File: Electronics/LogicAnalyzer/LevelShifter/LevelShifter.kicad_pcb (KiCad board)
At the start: 2 copper layers, 28.3 x 39.8 mm, 20 parts, among them J1 Conn_02x15_Odd_Even, J2 Conn_02x15_Odd_Even, U1 TXU0104PWR, U2 TXU0104PWR, U3 TXU0104PWR, U4 TXU0104PWR, U5 TXU0104PWR, U6 TXU0104PWR

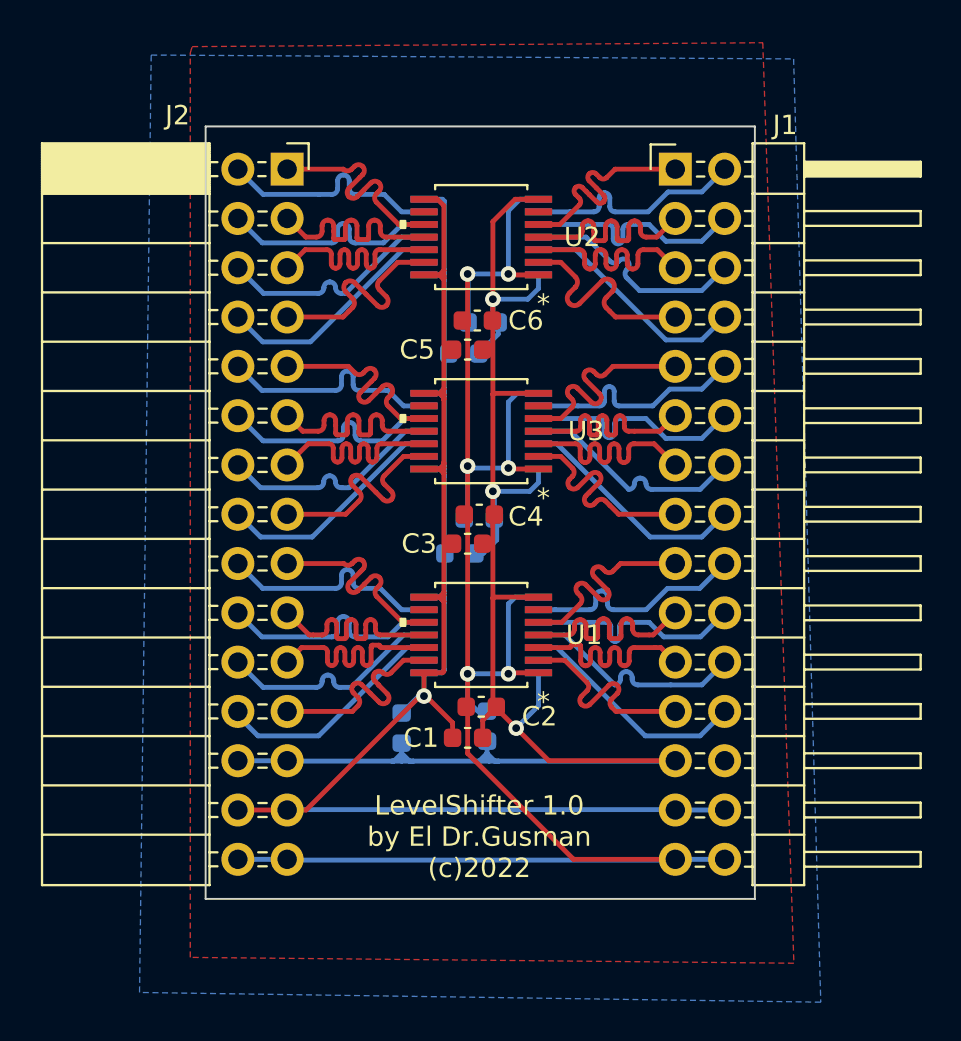
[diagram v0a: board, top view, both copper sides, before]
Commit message: Updated shifter board
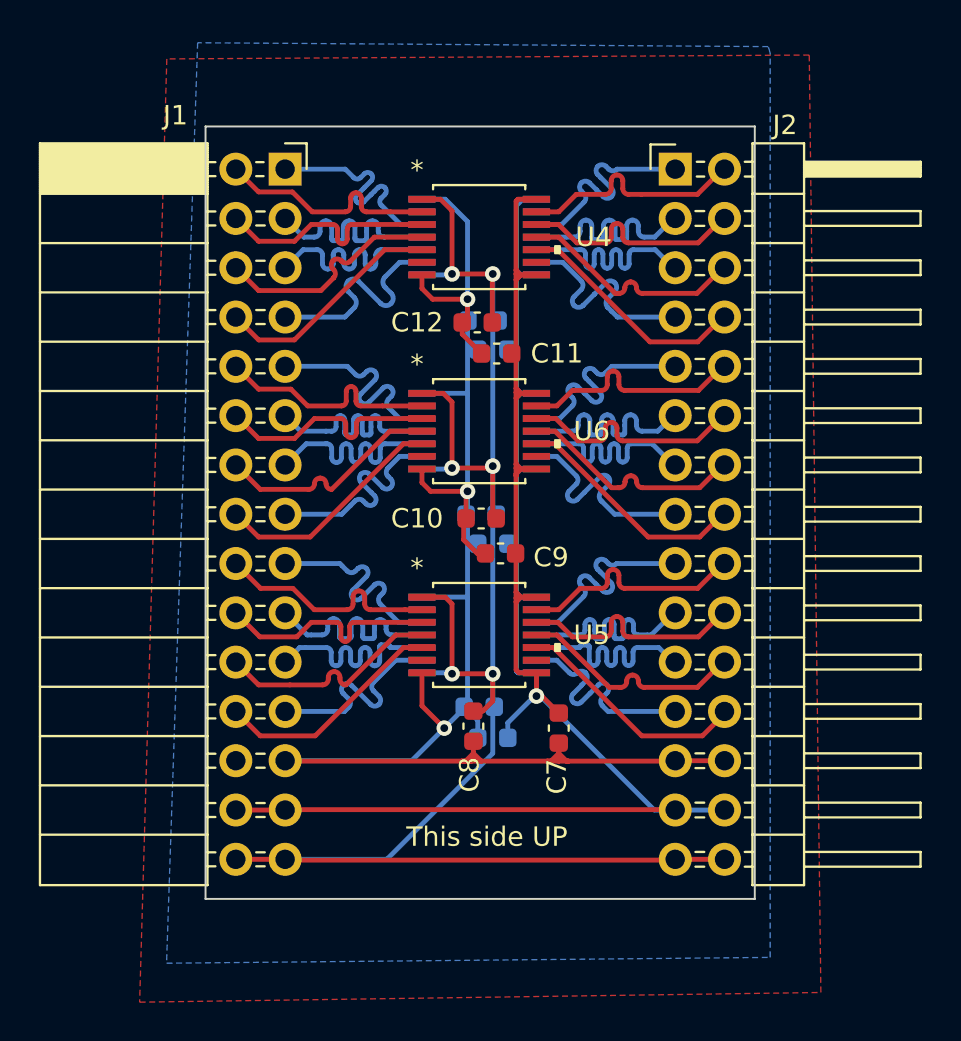
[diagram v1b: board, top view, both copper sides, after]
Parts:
- C1, C2, C3, C4, C5, C6, U1, U2, U3: moved to B.Cu
- C10, C11, C12, C7, C8, C9, U4, U5, U6: moved to F.Cu
- J1: footprint Connector_PinHeader_2.54mm:PinHeader_2x15_P2.54mm_Horizontal -> Connector_PinSocket_2.54mm:PinSocket_2x15_P2.54mm_Horizontal
- J2: footprint Connector_PinSocket_2.54mm:PinSocket_2x15_P2.54mm_Horizontal -> Connector_PinHeader_2.54mm:PinHeader_2x15_P2.54mm_Horizontal
- moved J1 20.1 mm to (149.9, 80.0)
- moved J2 20.0 mm to (170.0, 80.0)
- moved C7 8.09 mm to (164.0, 108.8)
- moved C9 2.09 mm to (161.0, 99.8), turned to 180 degrees
- moved C11 1.69 mm to (160.8, 89.5), turned to 180 degrees
- moved C1 1.29 mm to (160.6, 109.3), turned to 180 degrees
- moved C3 1.29 mm to (160.6, 99.3), turned to 180 degrees
- moved C5 1.29 mm to (160.6, 89.3), turned to 180 degrees
- moved C8 0.71 mm to (159.6, 108.7)
- moved C12 0.31 mm to (159.8, 87.9), turned to 0 degrees
- moved C6 0.29 mm to (160.1, 87.8), turned to 0 degrees
- moved C2 0.10 mm to (159.9, 107.7), turned to 0 degrees
- moved U1 0.10 mm to (159.9, 104.0), turned to 0 degrees
- moved U2 0.10 mm to (159.9, 83.5), turned to 0 degrees
- moved U3 0.10 mm to (159.9, 93.5), turned to 0 degrees
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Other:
- board text added: "This side UP"

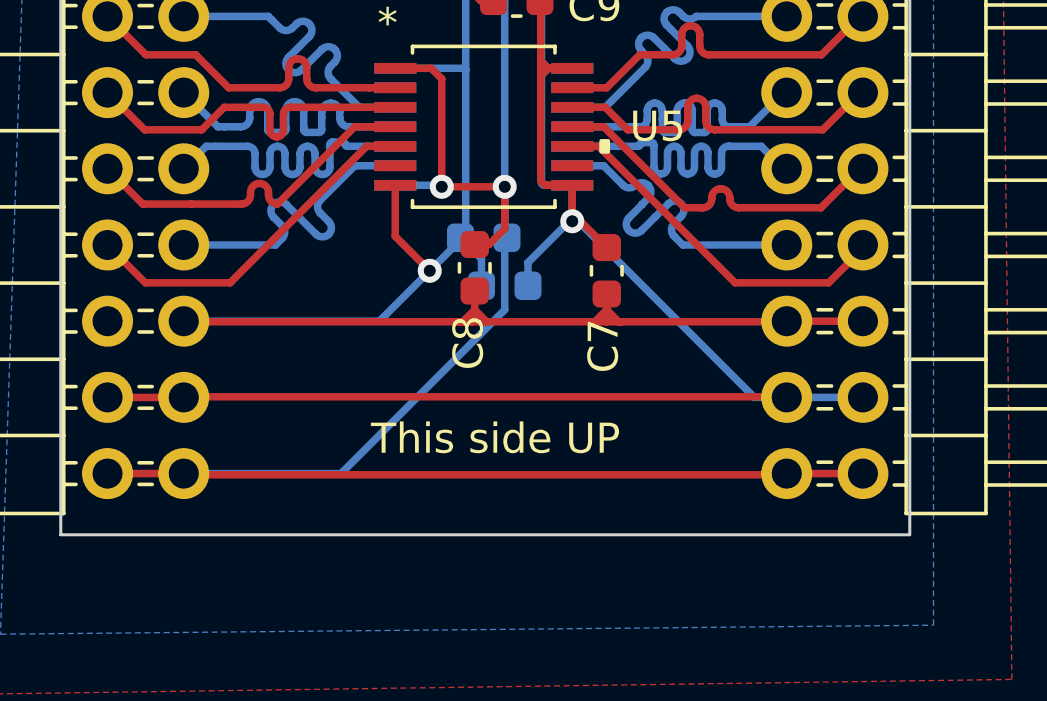
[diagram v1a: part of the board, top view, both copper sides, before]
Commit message: Updated LevelShifter with VRef selector
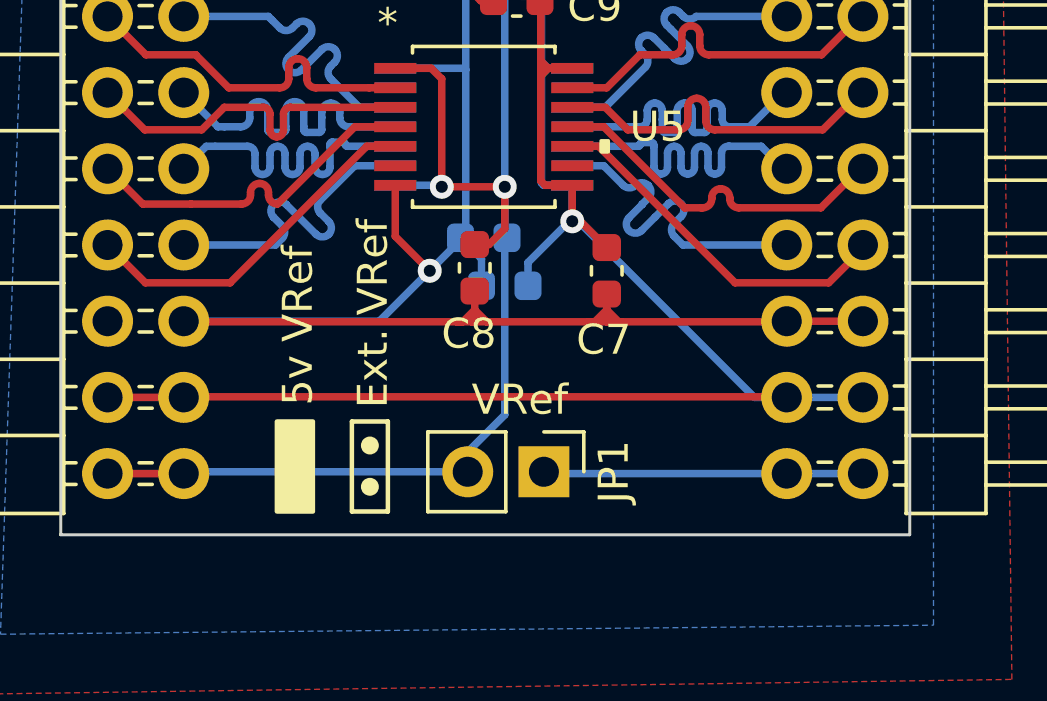
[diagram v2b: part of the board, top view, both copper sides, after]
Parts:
- added JP1: Conn_01x02, Connector_PinHeader_2.54mm:PinHeader_1x02_P2.54mm_Vertical, F.Cu at (161.9, 115.5)
- C1, C10, C11, C12, C2, C3, C4, C5, C6, C7, C8, C9: value C -> 100nf 16v
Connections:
- C10 pad 2: /5V -> /5V_VREF
- C12 pad 2: /5V -> /5V_VREF
- C2 pad 2: /5V -> /5V_VREF
- C4 pad 2: /5V -> /5V_VREF
- C6 pad 2: /5V -> /5V_VREF
- C8 pad 2: /5V -> /5V_VREF
- J1 pad 29: /5V -> /5V_VREF
- J1 pad 30: /5V -> /5V_VREF
- U1 pad 1: /5V -> /5V_VREF
- U2 pad 1: /5V -> /5V_VREF
- U3 pad 1: /5V -> /5V_VREF
- U4 pad 1: /5V -> /5V_VREF
- U5 pad 1: /5V -> /5V_VREF
- U6 pad 1: /5V -> /5V_VREF
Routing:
- net /5V: track 97.2 -> 10.7 mm, vias 6 -> 0
- net /5V_VREF: track 0.00 -> 77.1 mm, vias 0 -> 6
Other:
- board text added: "5v VRef"
- board text added: "Ext. VRef"
- board text added: "VRef"
- board text removed: "This side UP"

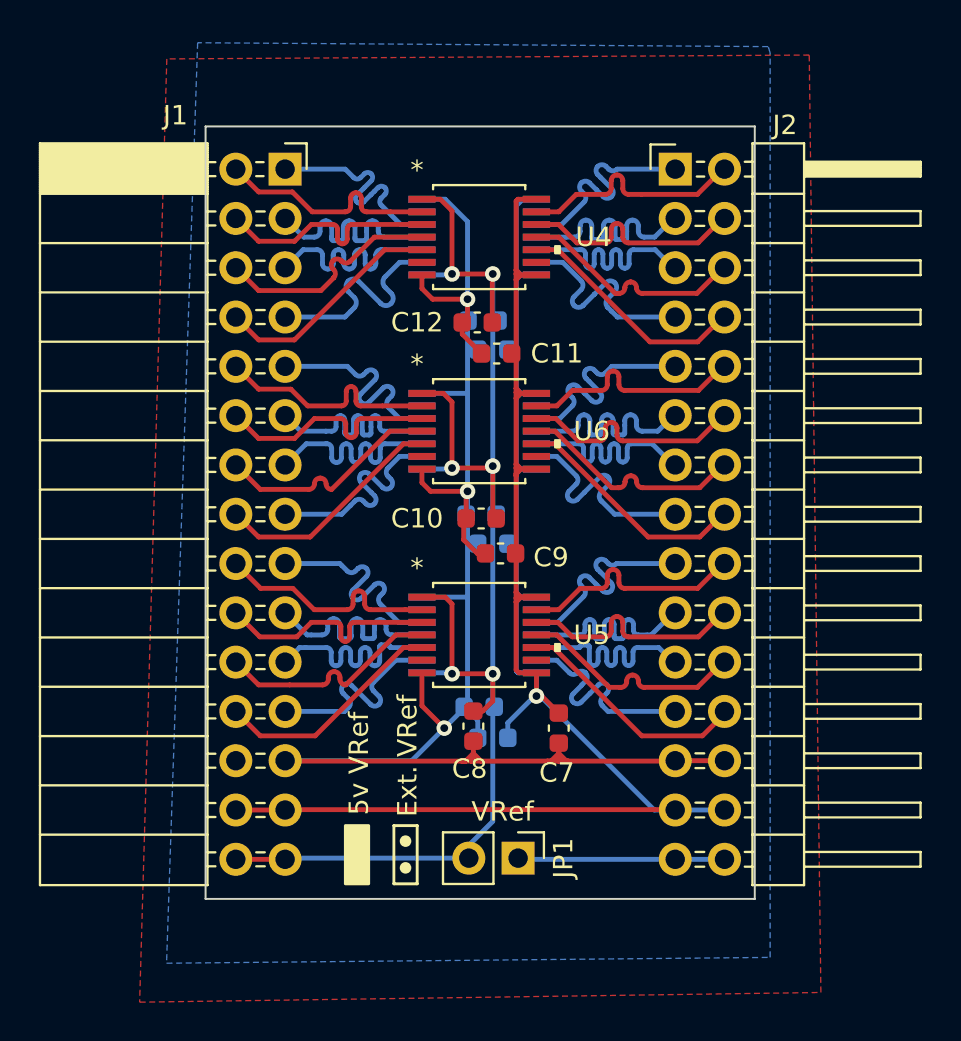
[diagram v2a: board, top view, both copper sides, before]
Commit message: New external trigger
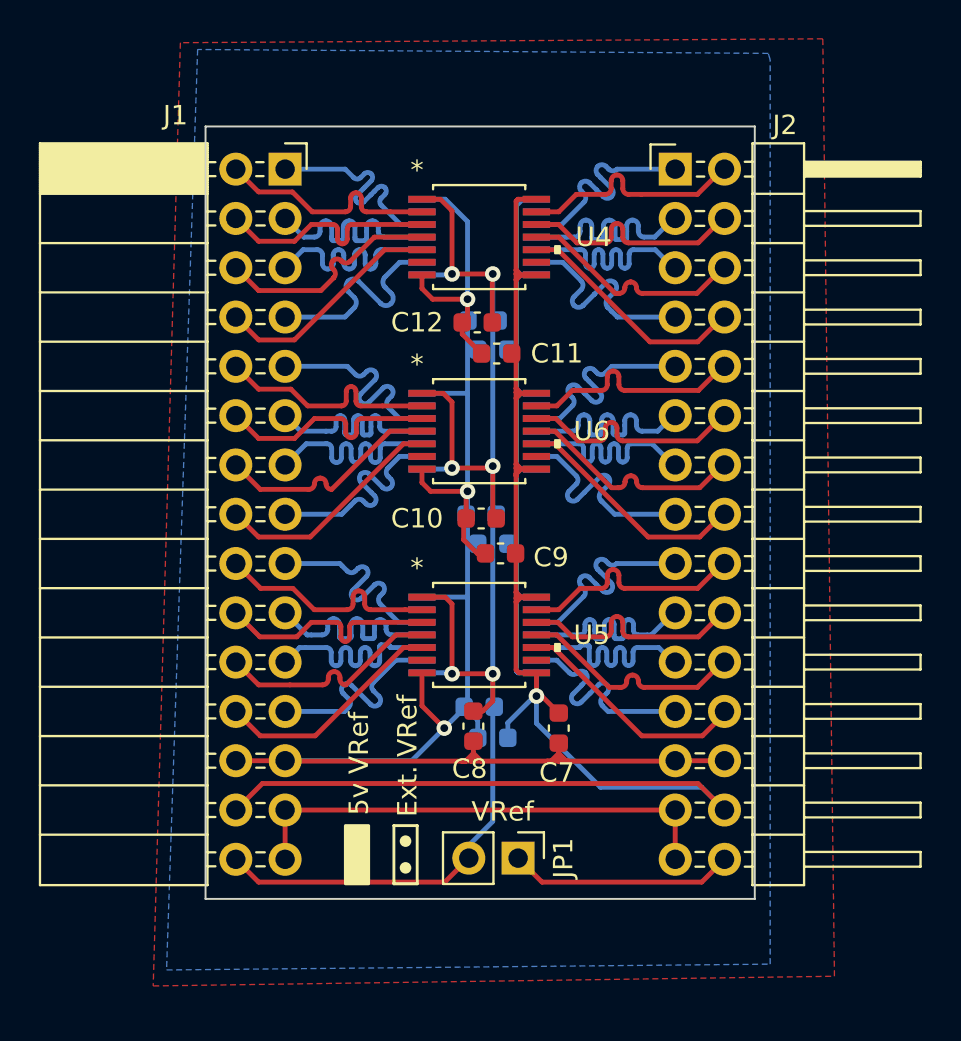
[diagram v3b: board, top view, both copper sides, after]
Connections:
- J1 pad 27: /3V3 -> /EXT_T
- J1 pad 29: /5V_VREF -> /EXT_T
- J2 pad 27: /3V3 -> /EXT_T
- J2 pad 29: /5V -> /EXT_T
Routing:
- net /EXT_T: track 0.00 -> 25.2 mm
- net /3V3: track 108.0 -> 112.7 mm
- net /GND: track 89.4 -> 92.0 mm
- net /5V_VREF: track 77.1 -> 78.0 mm
- net /5V: track 10.7 -> 11.6 mm

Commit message: Updated pcb texts to new version
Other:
- board text added: "LevelShifter 1.5 by El Dr.Gusman (c)2022"
- board text removed: "LevelShifter 1.0 by El Dr.Gusman (c)2022"
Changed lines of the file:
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@@
   (gr_circle (center 156.1 116) (end 156.323607 116) (layer "F.SilkS") (width 0.15) (fill solid))
   (gr_rect (start 145.795 117.6) (end 174.095 77.8) (layer "Edge.Cuts") (width 0.1) (fill none))
-  (gr_text "LevelShifter 1.0\nby El Dr.Gusman\n(c)2022" (at 160.6 112.3) (layer "B.SilkS")
+  (gr_text "LevelShifter 1.5\nby El Dr.Gusman\n(c)2022" (at 160.6 112.3) (layer "B.SilkS")
     (effects (font (size 0.5 0.5) (thickness 0.1)) (justify mirror))
   )
